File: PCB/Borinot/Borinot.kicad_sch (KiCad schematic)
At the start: 31 parts, among them J1 USB_C_Receptacle_USB2.0, J2 Battery, J3 HumiditySensor, U1 MCP73871-2CC

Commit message: Four-layer board
Moved the design to a four-layer board, to simplify routing.
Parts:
- removed R6, R7, R8: 470, Resistor_SMD:R_0805_2012Metric_Pad1.20x1.40mm_HandSolder, symbol Device:R
- added SW1: RESET, Button_Switch_THT:SW_PUSH_6mm, symbol Switch:SW_Push
- added SW2: PROG, Button_Switch_THT:SW_PUSH_6mm, symbol Switch:SW_Push
- U1: footprint Package_DFN_QFN:QFN-20-1EP_4x4mm_P0.5mm_EP2.5x2.5mm -> Package_DFN_QFN:TQFN-20-1EP_4x4mm_P0.5mm_EP2.7x2.7mm_ThermalVias
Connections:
- net ESP_EN: now also SW1.1
- net ESP_SDA: now also J3.1 (Pin_1); no longer J3.4 (Pin_4)
- net GND: now also SW1.2, SW2.2
- net USB_5V: no longer U2.3 (STBY)
- net VDD33: now also J3.4 (Pin_4); no longer J3.1 (Pin_1)
- net GPIO0: now reaches U3.27 (IO0)
- net GPIO0: now also SW2.1
- net BAT_OUT: now reaches C1.1, C5.1, U1.1 (OUT), U1.20 (OUT), U2.1 (VIN)
- net BAT_OUT: now also U2.3 (STBY)
- no-connect marks 29 -> 28
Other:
- note added: "* Monitor battery voltage. * Use an easier-to-solder battery manager * Could use a simpler MCP... without load sharing"
- moved on the sheet: C1, C2, C3, C4, C5, C6, C7, C8, D1, D2, H1, H2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

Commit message: Battery management change
Use an easier-to-solder SOT-23-5-packaged battery manager
to simplify the soldeering of the PCBs.
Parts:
- removed C3, C5: 4.7uF, Capacitor_SMD:C_0805_2012Metric_Pad1.18x1.45mm_HandSolder, symbol Device:C_Small
- removed C4: 1uF, Capacitor_SMD:C_0805_2012Metric_Pad1.18x1.45mm_HandSolder, symbol Device:C_Small
- removed J2: Battery, Connector_Molex:Molex_KK-254_AE-6410-03A_1x03_P2.54mm_Vertical, symbol Connector_Generic:Conn_01x03
- removed R4: 10k, Resistor_SMD:R_0805_2012Metric_Pad1.20x1.40mm_HandSolder, symbol Device:R
- removed R5: 12k5, Resistor_SMD:R_0805_2012Metric_Pad1.20x1.40mm_HandSolder, symbol Device:R
- removed U1: MCP73871-2CC, Package_DFN_QFN:TQFN-20-1EP_4x4mm_P0.5mm_EP2.7x2.7mm_ThermalVias, symbol Battery_Management:MCP73871-2CC
- added J3: Battery, Connector_PinHeader_2.54mm:PinHeader_1x02_P2.54mm_Vertical, symbol Connector_Generic:Conn_01x02
- added R6: 2k, Resistor_SMD:R_0805_2012Metric_Pad1.20x1.40mm_HandSolder, symbol Device:R
- added R7, R8: 100k, Resistor_SMD:R_0805_2012Metric_Pad1.20x1.40mm_HandSolder, symbol Device:R
- added U1: MCP73812T-420I-OT, Package_TO_SOT_SMD:SOT-23-5, symbol Battery_Management:MCP73812T-420I-OT
- C2: value 10uF -> 1uF
- renumbered C6 to C3, C7 to C4, C8 to C5, H2 to H1, H1 to H2, J3 to J1, J1 to J2, R12 to R10, R13 to R11, R9 to R2, R2 to R3, R10 to R4, R3 to R5, R11 to R9, SW2 to SW1, SW1 to SW2
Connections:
- net BAT_OUT is gone; now on net VBAT: C1.1, U2.1 (VIN), U2.3 (STBY)
- net GND: now also J3.2 (Pin_2), R6.2, R8.2, U1.2 (V_{SS})
- net USB_5V: now also U1.4 (V_{DD}); no longer C2.1
- net VBAT: now also J3.1 (Pin_1), R7.1, U1.3 (V_{BAT})
- net VDD33: now also C2.1
- net BAT_SENSE: now reaches U3.4 (IO4)
- net BAT_SENSE: now also R7.2, R8.1
- net BAT_CE: now reaches U3.7 (IO7)
- net BAT_CE: now also U1.1 (CE)
- net BAT_STAT2: no longer names the net of U3.35 (IO42)
- net ~{BAT_LBO}: no longer names the net of U3.34 (IO41)
- net ~{BAT_PG}: no longer names the net of U3.33 (IO40)
- new net: R6.1, U1.5 (PROG)
- no-connect marks 28 -> 29
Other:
- note removed: "* Monitor battery voltage. * Use an easier-to-solder battery manager * Could use a simpler MCP... without load sharing"
- note removed: "Charging cut-off current of 80 mA."
- note removed: "PROG2: Select 450 mA of charge current instead of just 90 mA"
- note removed: "Preconditioning current of 100 mA"
- note removed: "SELect USB input charging instead of AC"
- moved on the sheet: C3, C4, C5, D1, D2, R10, R11, R2, R4, R9, SW1, SW2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

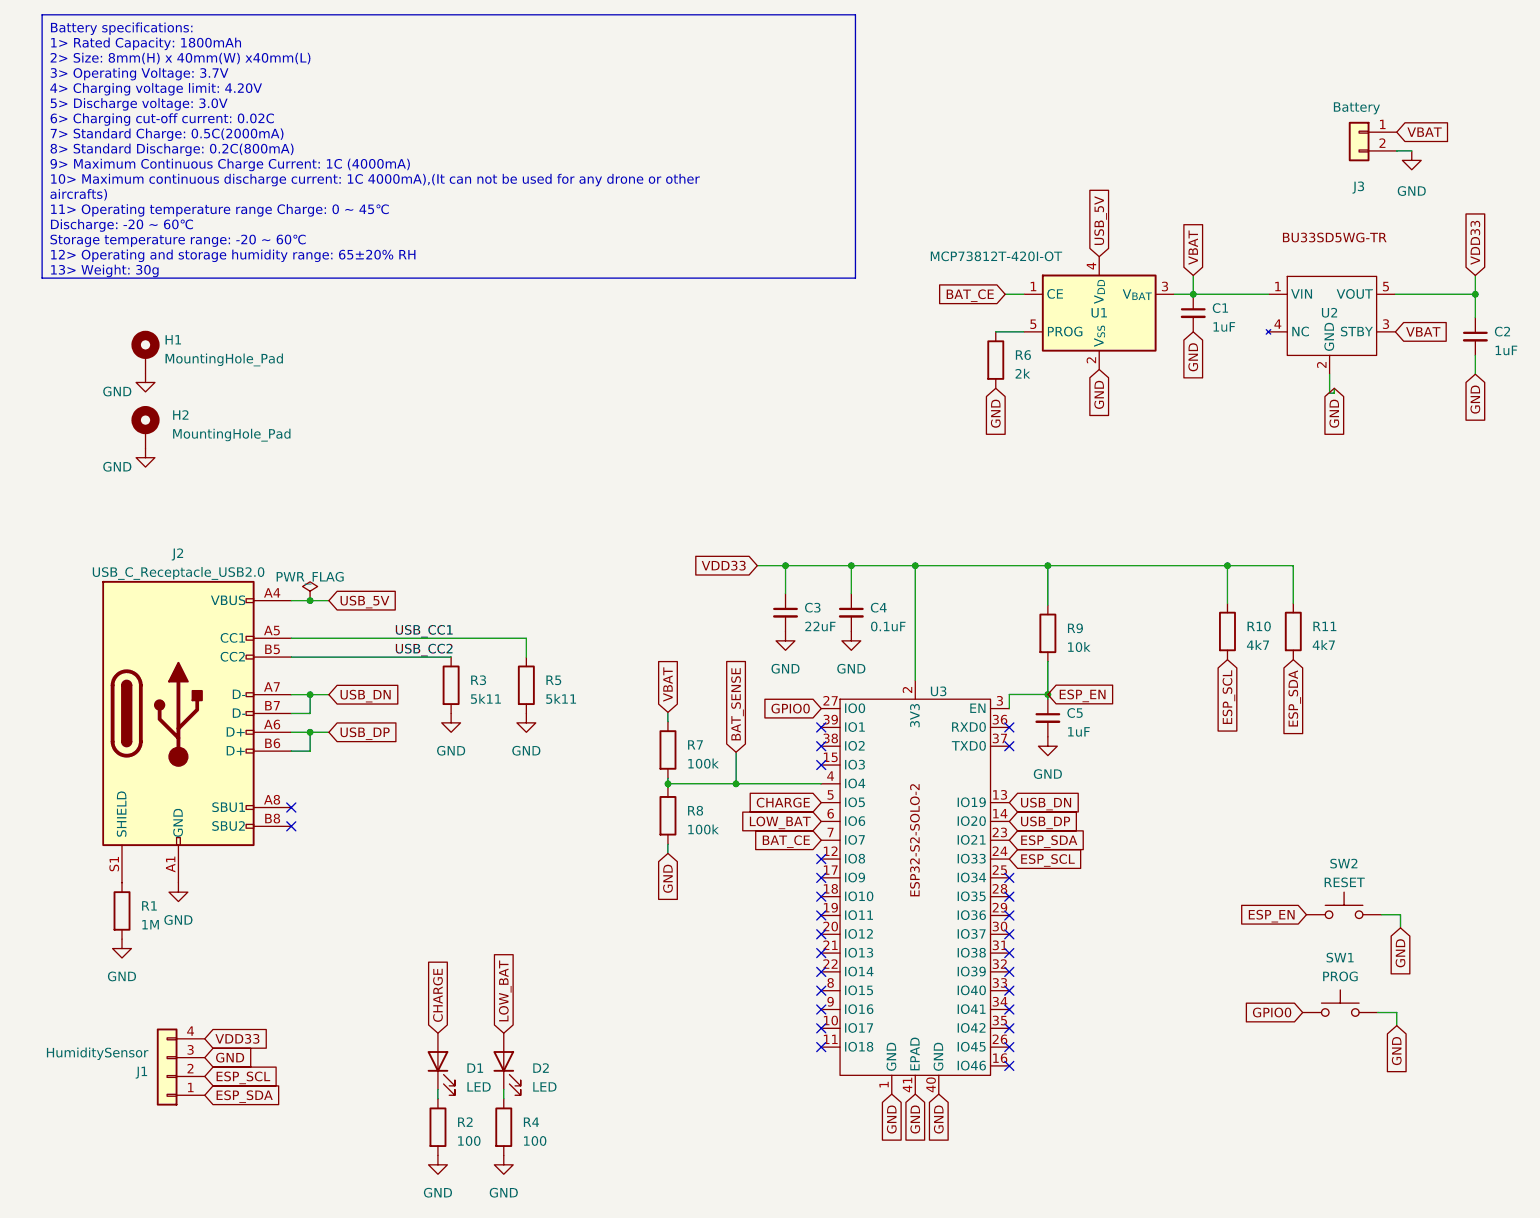
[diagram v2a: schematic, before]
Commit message: Add missing pull-up on ChargeEnable pin
Without a pull-up to USB 5V on that pin it is impossible
to start the ESP32 when the battery is below 3.3V
Added a voltage divider to sense the 5V from USB and
be able to decide whether to charge the battery or not.
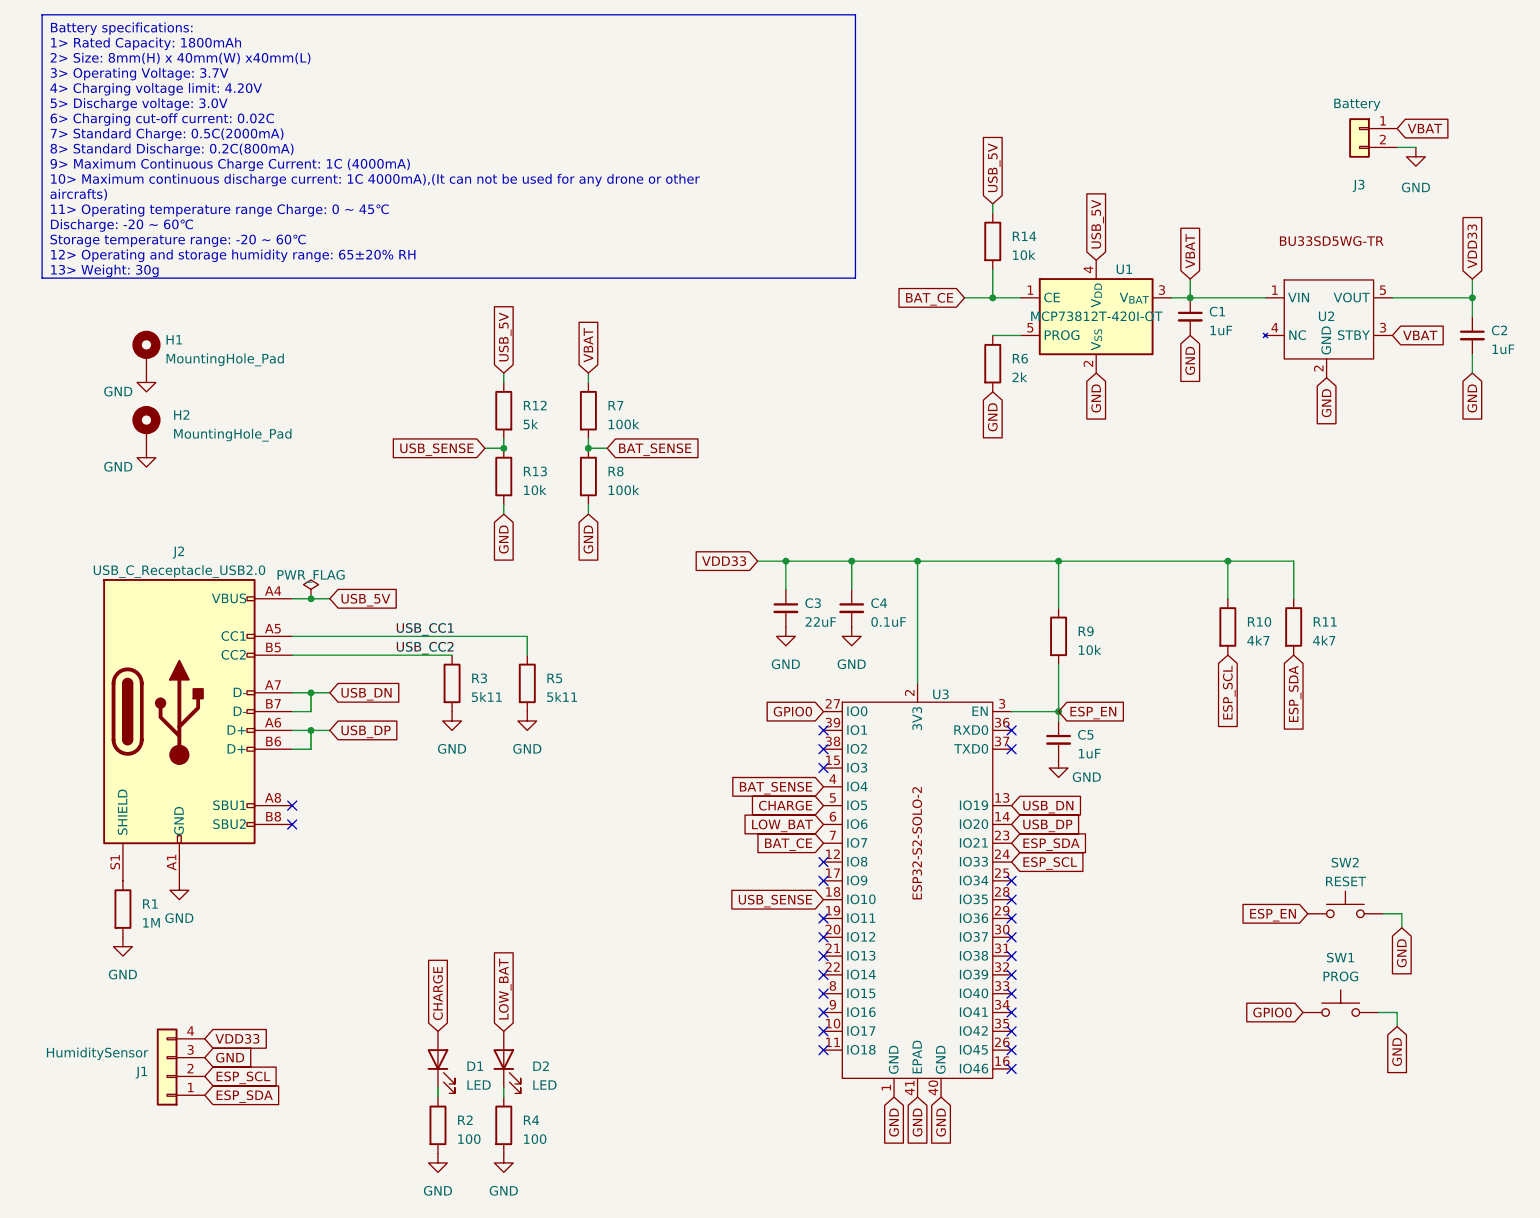
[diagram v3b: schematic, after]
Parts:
- added R12: 5k, Resistor_SMD:R_0805_2012Metric_Pad1.20x1.40mm_HandSolder, symbol Device:R
- added R13, R14: 10k, Resistor_SMD:R_0805_2012Metric_Pad1.20x1.40mm_HandSolder, symbol Device:R
- D1, D2: footprint LED_THT:LED_D3.0mm -> LED_SMD:LED_0805_2012Metric
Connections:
- net BAT_CE: now also R14.2
- net GND: now also R13.2
- net USB_5V: now also R12.1, R14.1
- net USB_SENSE: now reaches U3.18 (IO10)
- net USB_SENSE: now also R12.2, R13.1
- no-connect marks 29 -> 28
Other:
- moved on the sheet: C1, C3, C4, C5, R10, R11, R6, R7, R8, R9, U1, U2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
